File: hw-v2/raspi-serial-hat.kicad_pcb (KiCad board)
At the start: 2 copper layers, 65 x 56.5 mm, 41 parts, among them J1 Conn_02x10_Odd_Even, J2 DB9_Male, J3 DB9_Male, U1 DS3231, U2 MAX3109, U3 MCP23S17, U4 LT1137ACSW

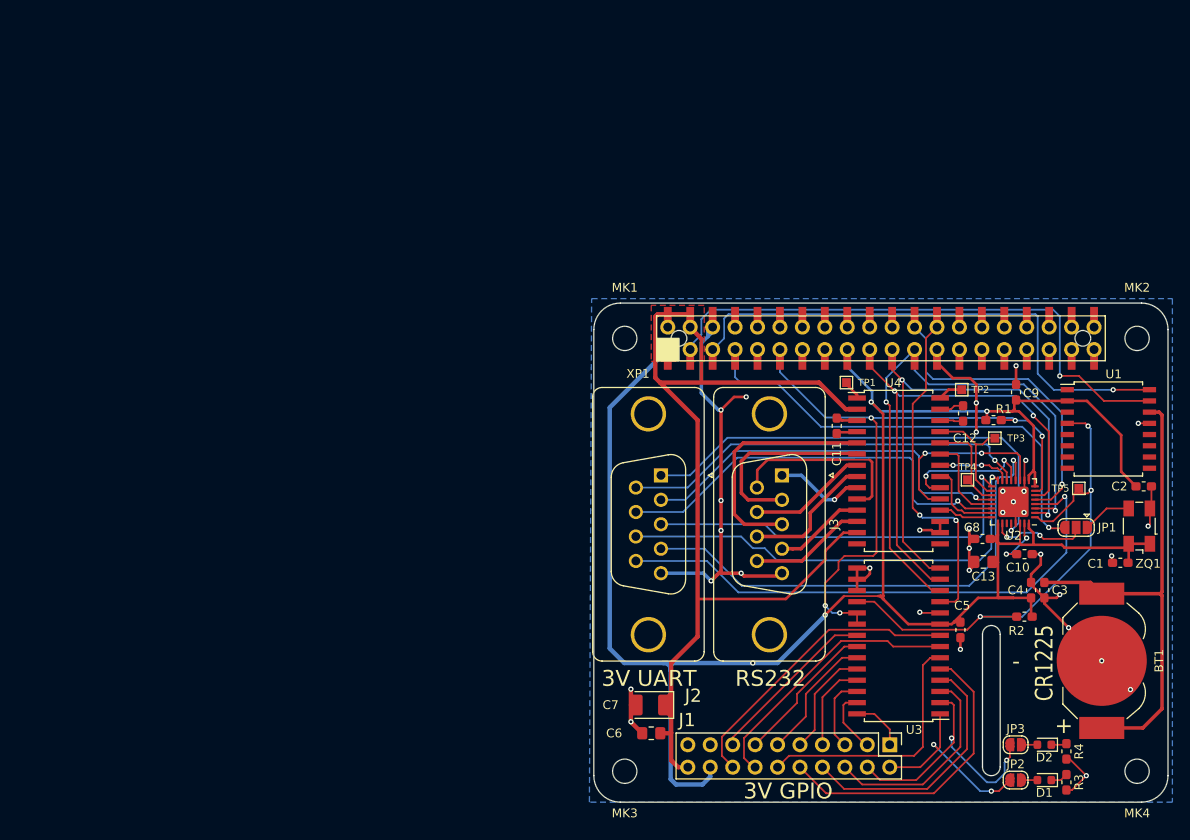
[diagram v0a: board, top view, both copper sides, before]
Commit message: board v2, using IDC cables and with config rom.
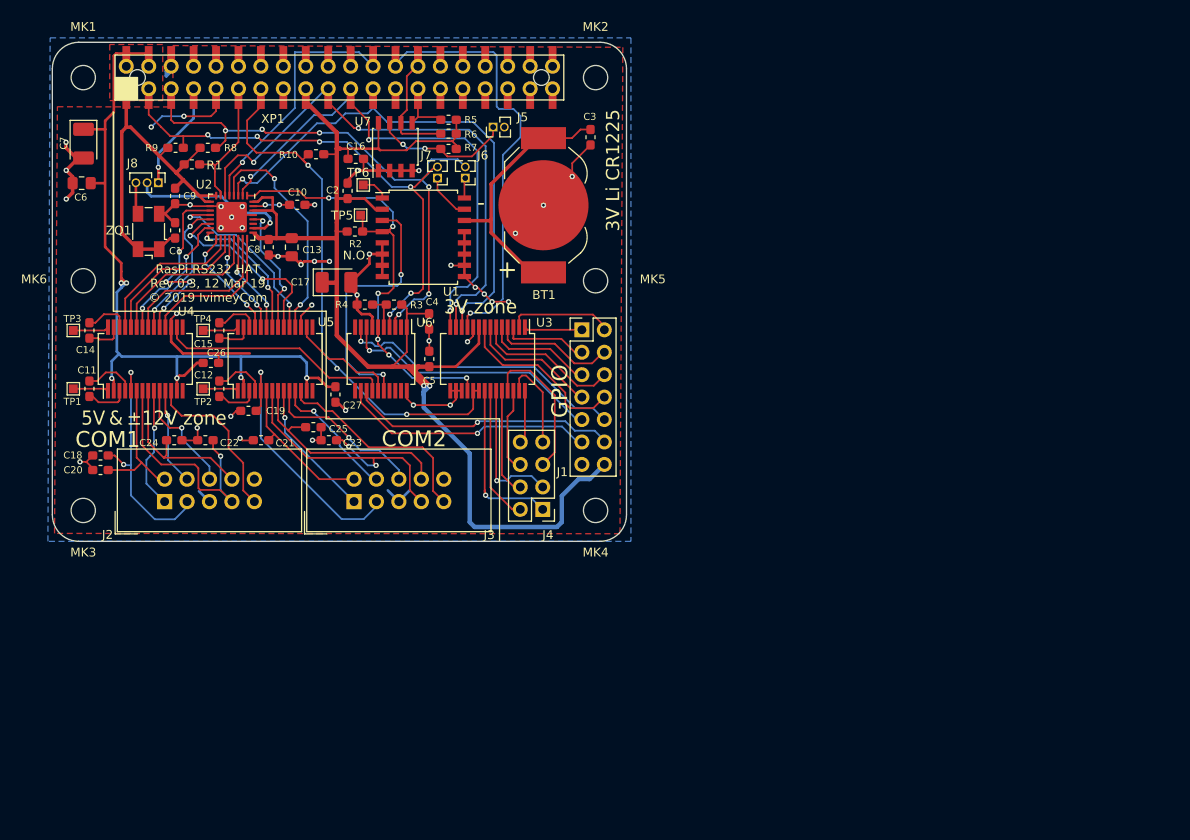
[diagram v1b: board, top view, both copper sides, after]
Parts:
- removed D1, D2: LED, Diode_SMD:D_0603_1608Metric
- removed JP1: CLK Source, Jumper:SolderJumper-3_P1.3mm_Open_RoundedPad1.0x1.5mm
- removed JP2: LED1 Enable, Jumper:SolderJumper-2_P1.3mm_Open_RoundedPad1.0x1.5mm
- removed JP3: LED2 Enable, Jumper:SolderJumper-2_P1.3mm_Open_RoundedPad1.0x1.5mm
- added C14: 100nF, Capacitor_SMD:C_0603_1608Metric_Pad1.05x0.95mm_HandSolder, F.Cu at (38.1, 63.7)
- added C15: 100nF, Capacitor_SMD:C_0603_1608Metric_Pad1.05x0.95mm_HandSolder, F.Cu at (52.8, 63.7)
- added C16: 100nF, Capacitor_SMD:C_0603_1608Metric_Pad1.05x0.95mm_HandSolder, F.Cu at (68.2, 44.3)
- added C17: 100uF, Capacitor_Tantalum_SMD:CP_EIA-3528-12_Kemet-T_Pad1.50x2.35mm_HandSolder, F.Cu at (66.1, 58.2)
- added C18: 100pF, Capacitor_SMD:C_0603_1608Metric_Pad1.05x0.95mm_HandSolder, F.Cu at (39.4, 77.8)
- added C19: 100pF, Capacitor_SMD:C_0603_1608Metric_Pad1.05x0.95mm_HandSolder, F.Cu at (56.1, 72.8)
- added C20: 100pF, Capacitor_SMD:C_0603_1608Metric_Pad1.05x0.95mm_HandSolder, F.Cu at (39.4, 79.5)
- added C21: 100pF, Capacitor_SMD:C_0603_1608Metric_Pad1.05x0.95mm_HandSolder, F.Cu at (57.5, 76.1)
- added C22: 100pF, Capacitor_SMD:C_0603_1608Metric_Pad1.05x0.95mm_HandSolder, F.Cu at (51.2, 76.1)
- added C23: 100pF, Capacitor_SMD:C_0603_1608Metric_Pad1.05x0.95mm_HandSolder, F.Cu at (65.2, 76.1)
- added C24: 100pF, Capacitor_SMD:C_0603_1608Metric_Pad1.05x0.95mm_HandSolder, F.Cu at (47.7, 76.1)
- added C25: 100pF, Capacitor_SMD:C_0603_1608Metric_Pad1.05x0.95mm_HandSolder, F.Cu at (63.5, 74.7)
- added C26: 100nF, Capacitor_SMD:C_0603_1608Metric_Pad1.05x0.95mm_HandSolder, F.Cu at (51.9, 67.4)
- added C27: 100nF, Capacitor_SMD:C_0603_1608Metric_Pad1.05x0.95mm_HandSolder, F.Cu at (66.0, 71.0)
- added J4: Conn_02x04, Connector_PinHeader_2.54mm:PinHeader_2x04_P2.54mm_Vertical, F.Cu at (89.4, 84.0)
- added J5: Conn_01x02, Connector_PinHeader_1.27mm:PinHeader_1x02_P1.27mm_Vertical, F.Cu at (83.8, 40.7)
- added J6: Conn_01x02, Connector_PinHeader_1.27mm:PinHeader_1x02_P1.27mm_Vertical, F.Cu at (80.7, 46.5)
- added J7: Conn_01x02, Connector_PinHeader_1.27mm:PinHeader_1x02_P1.27mm_Vertical, F.Cu at (77.5, 46.5)
- added J8: Conn_01x03, Connector_PinHeader_1.27mm:PinHeader_1x03_P1.27mm_Vertical, F.Cu at (45.9, 47.0)
- added MK5: MountingHole, hat:M2.5_Mounting_Hole, F.Cu at (95.4, 58.1)
- added MK6: MountingHole, hat:M2.5_Mounting_Hole, F.Cu at (37.4, 58.1)
- added R10: 10K, Resistor_SMD:R_0603_1608Metric_Pad1.05x0.95mm_HandSolder, F.Cu at (63.8, 43.8)
- added R5: 3.9K, Resistor_SMD:R_0603_1608Metric_Pad1.05x0.95mm_HandSolder, F.Cu at (78.8, 39.9)
- added R6: 3.9K, Resistor_SMD:R_0603_1608Metric_Pad1.05x0.95mm_HandSolder, F.Cu at (78.8, 41.4)
- added R7: 1K, Resistor_SMD:R_0603_1608Metric_Pad1.05x0.95mm_HandSolder, F.Cu at (78.8, 43.1)
- added R8: 3.9K, Resistor_SMD:R_0603_1608Metric_Pad1.05x0.95mm_HandSolder, F.Cu at (51.5, 43.0)
- added R9: 3.9K, Resistor_SMD:R_0603_1608Metric_Pad1.05x0.95mm_HandSolder, F.Cu at (47.9, 43.0)
- added TP6: TestPoint, TestPoint:TestPoint_Pad_1.0x1.0mm, F.Cu at (69.1, 47.2)
- added U5: LT1137ACG, Package_SO:SSOP-28_5.3x10.2mm_P0.65mm, F.Cu at (59.1, 66.9)
- added U6: MCP23009_SS, Package_SO:SSOP-20_5.3x7.2mm_P0.65mm, F.Cu at (71.1, 66.9)
- added U7: CAT24C64, Package_SO:SOIC-8_3.9x4.9mm_P1.27mm, F.Cu at (72.7, 42.9)
- BT1: value CR1225 -> Battery_Cell
- C11, C12: value 0.1uF -> 100nF
- C13, C6: value 10uF Ceramic -> 10uF
- C2, C4, C5: value 1uF -> 100nF
- C3: value 470nF -> 100nF
- C7: value 100uF Tant -> 100uF
- J1: value Conn_02x10_Odd_Even -> Conn_02x07; footprint Connector_PinHeader_2.54mm:PinHeader_2x10_P2.54mm_Vertical -> Connector_PinHeader_2.54mm:PinHeader_2x07_P2.54mm_Vertical
- J2, J3: value DB9_Male -> Conn_02x05_Odd_Even; footprint Connector_Dsub:DSUB-9_Male_Vertical_P2.77x2.84mm_MountingHoles -> Connector_IDC:IDC-Header_2x05_P2.54mm_Vertical
- MK1, MK2, MK3, MK4: value Mounting_Hole -> MountingHole
- R1: value 10k -> 10K
- R2: value nc -> NO
- R3, R4: value 470 -> 10K
- U3: value MCP23S17 -> MCP23S17_SS; footprint Package_SO:SOIC-28W_7.5x17.9mm_P1.27mm -> Package_SO:SSOP-28_5.3x10.2mm_P0.65mm
- U4: value LT1137ACSW -> LT1137ACG; footprint Package_SO:SOIC-28W_7.5x17.9mm_P1.27mm -> Package_SO:SSOP-28_5.3x10.2mm_P0.65mm
- ZQ1: value ASFL1-24.000MHZ-EC-T -> ASFL1-oscillator
- moved ZQ1 117.0 mm to (44.8, 52.5)
- moved C1 113.4 mm to (47.8, 52.4), turned to 90 degrees
- moved TP3 105.0 mm to (36.3, 63.7)
- moved C9 97.8 mm to (47.8, 48.5), turned to 270 degrees
- moved C2 96.1 mm to (67.3, 47.9), turned to 90 degrees
- moved R1 95.3 mm to (49.7, 44.9)
- moved U2 94.2 mm to (54.2, 50.9), turned to 270 degrees
- moved R4 94.2 mm to (69.3, 60.8), turned to 0 degrees
- moved R3 93.4 mm to (72.6, 60.8), turned to 0 degrees
- moved C10 91.3 mm to (61.6, 49.5)
- moved C7 90.3 mm to (37.4, 42.5), turned to 270 degrees
- moved C6 89.6 mm to (37.2, 47.0)
- moved TP4 88.2 mm to (51.0, 63.7)
- moved TP1 87.5 mm to (36.3, 70.3)
- moved R2 87.4 mm to (68.2, 52.5), turned to 180 degrees
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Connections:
- net /V+ renamed /V0+
- net RPI_SPI0_MISO renamed /MISO
- net RPI_SPI0_MOSI renamed /MOSI
- net RPI_SPI0_SCLK renamed /SCLK
- J1 pad 1: Net-(J1-Pad1) -> /PB0
- J1 pad 10: Net-(J1-Pad10) -> /PC1
- J1 pad 11: Net-(J1-Pad11) -> /PC2
- J1 pad 12: Net-(J1-Pad12) -> /PC3
- J1 pad 13: Net-(J1-Pad13) -> GND
- J1 pad 14: Net-(J1-Pad14) -> +3V3
- J1 pad 2: Net-(J1-Pad2) -> /PB1
- J1 pad 3: Net-(J1-Pad3) -> /PB2
- J1 pad 4: Net-(J1-Pad4) -> /PB3
- J1 pad 5: Net-(J1-Pad5) -> /PB4
- J1 pad 6: Net-(J1-Pad6) -> /PB5
- J1 pad 7: Net-(J1-Pad7) -> /PB6
- J1 pad 8: Net-(J1-Pad8) -> /PB7
- J1 pad 9: Net-(J1-Pad9) -> /PC0
- J2 pad 1: /~U1_DCD -> /~E0_DCD
- J2 pad 2: /U1_RX -> /E0_RX
- J2 pad 3: /U1_TX -> /E0_TX
- J2 pad 4: /~U1_DTR -> /~E0_DTR
- J2 pad 6: /~U1_DSR -> /~E0_DSR
- J2 pad 7: /~U1_RTS -> /~E0_RTS
- J2 pad 8: /~U1_CTS -> /~E0_CTS
- J2 pad 9: /~U1_RI -> /~E0_RI
- J3 pad 1: /E_DCD -> /~E1_DCD
- J3 pad 2: /E_RX -> /E1_RX
- J3 pad 3: /E_TX -> /E1_TX
- J3 pad 4: /E_DTR -> /~E1_DTR
- J3 pad 6: /E_DSR -> /~E1_DSR
- J3 pad 7: /E_RTS -> /~E1_RTS
- J3 pad 8: /E_CTS -> /~E1_CTS
- J3 pad 9: /E_RI -> /~E1_RI
- R3 pad 1: Net-(D1-Pad1) -> Net-(R3-Pad1)
- R3 pad 2: GND -> +3V3
- R4 pad 1: Net-(D2-Pad1) -> GND
- R4 pad 2: GND -> Net-(R3-Pad1)
- TP2 pad 1: /V- -> /V1+
- TP3 pad 1: /U0_TX -> /V0-
- TP4 pad 1: /U0_RX -> /V1-
- U1 pad 1: (no net) -> Net-(TP6-Pad1)
- U1 pad 10: (no net) -> GND
- U1 pad 11: (no net) -> GND
- U1 pad 12: (no net) -> GND
- U1 pad 15: RPI_SDA -> Net-(J7-Pad1)
- U1 pad 16: RPI_SCL -> Net-(J6-Pad1)
- U1 pad 3: (no net) -> CLK_INT_SW
- U1 pad 5: (no net) -> GND
- U1 pad 6: (no net) -> GND
- U1 pad 7: (no net) -> GND
- U1 pad 8: (no net) -> GND
- U1 pad 9: (no net) -> GND
- U3 pad 1: Net-(J1-Pad2) -> /PB0
- U3 pad 19: ~SER_IRQ_A -> ~SER_IRQ_B
- U3 pad 2: Net-(J1-Pad4) -> /PB1
- U3 pad 20: ~SER_IRQ_A -> ~SER_IRQ_B
- U3 pad 21: Net-(J1-Pad15) -> /PA0
- U3 pad 22: Net-(J1-Pad13) -> /PA1
- U3 pad 23: Net-(J1-Pad11) -> /PA2
- U3 pad 24: Net-(J1-Pad9) -> /PA3
- U3 pad 25: Net-(J1-Pad7) -> /PA4
- U3 pad 26: Net-(J1-Pad5) -> /PA5
- U3 pad 27: Net-(J1-Pad3) -> /PA6
- U3 pad 28: Net-(J1-Pad1) -> /PA7
- U3 pad 3: Net-(J1-Pad6) -> /PB2
- U3 pad 4: Net-(J1-Pad8) -> /PB3
- U3 pad 5: Net-(J1-Pad10) -> /PB4
- U3 pad 6: Net-(J1-Pad12) -> /PB5
- U3 pad 7: Net-(J1-Pad14) -> /PB6
- U3 pad 8: Net-(J1-Pad16) -> /PB7
- U4 pad 10: /E_DSR -> /~E0_DSR
- U4 pad 11: /E_DTR -> /~E0_DTR
- U4 pad 12: /E_RI -> /~E0_RI
- U4 pad 16: GND -> U0_DISABLE
- U4 pad 26: Net-(C12-Pad1) -> Net-(C14-Pad2)
- U4 pad 27: Net-(C12-Pad2) -> Net-(C14-Pad1)
- U4 pad 28: /V- -> /V0-
- U4 pad 5: /E_TX -> /E0_TX
- U4 pad 6: /E_RX -> /E0_RX
- U4 pad 7: /E_RTS -> /~E0_RTS
- U4 pad 8: /E_CTS -> /~E0_CTS
- U4 pad 9: /E_DCD -> /~E0_DCD
- XP1 pad 13: Net-(XP1-Pad13) -> ~SER_IRQ_B
- XP1 pad 27: Net-(XP1-Pad27) -> ID_SD
- XP1 pad 28: Net-(XP1-Pad28) -> ID_SC
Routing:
- net ~SER_IRQ_B: track 0.00 -> 63.1 mm, vias 0 -> 2
- net ~SER_IRQ_A: track 77.7 -> 16.7 mm, vias 5 -> 0
- net RPI_GPCLK0: track 55.2 -> 15.2 mm
- net /~U1_DCD: track 52.8 -> 14.7 mm, vias 1 -> 2
- net /~U1_RTS: track 48.1 -> 11.5 mm, vias 1 -> 2
- net /~U1_RI: track 62.2 -> 26.3 mm, vias 1 -> 2
- net /~U1_CTS: track 50.8 -> 15.5 mm, vias 1 -> 2
- net /~U1_DTR: track 56.0 -> 21.3 mm, vias 1 -> 2
- net Net-(J1-Pad10): track 34.6 -> 0.00 mm
- net Net-(J1-Pad16): track 33.9 -> 0.00 mm
- net +3V3: track 237.8 -> 204.4 mm, vias 4 -> 2
- net /PC1: track 0.00 -> 33.2 mm, vias 0 -> 1
- net /U1_RX: track 44.2 -> 11.7 mm, vias 1 -> 2
- net /U1_TX: track 45.4 -> 12.9 mm, vias 1 -> 2
- net /~E1_RTS: track 0.00 -> 32.4 mm, vias 0 -> 2
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- added copper zone on F.Cu, net GND
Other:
- outline, holes or cut-outs redrawn
- board text added: "3V Li CR1225"
- board text added: "3V zone"
- board text added: "5V & ±12V zone"
- board text added: "COM1"
- board text added: "COM2"
- board text added: "Camera cutout"
- board text added: "Display cutout"
- board text added: "E d g e o f R a s p b e r r y P i Z e r o"
- board text added: "GPIO"
- board text added: "N.O."
- board text added: "RasPi RS232 HAT Rev 0.3, 12 Mar 19 © 2019 IvimeyCom"
- board text removed: "(c) 2019 IvimeyCom"
- board text removed: "3V GPIO"
- board text removed: "3V UART"
- board text removed: "CR1225"
- board text removed: "RS232"
- board text removed: "RasPi RS232 Hat"
